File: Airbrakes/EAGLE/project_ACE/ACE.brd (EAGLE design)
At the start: 106.7 x 61 mm, 8 parts, among them J3 PTH

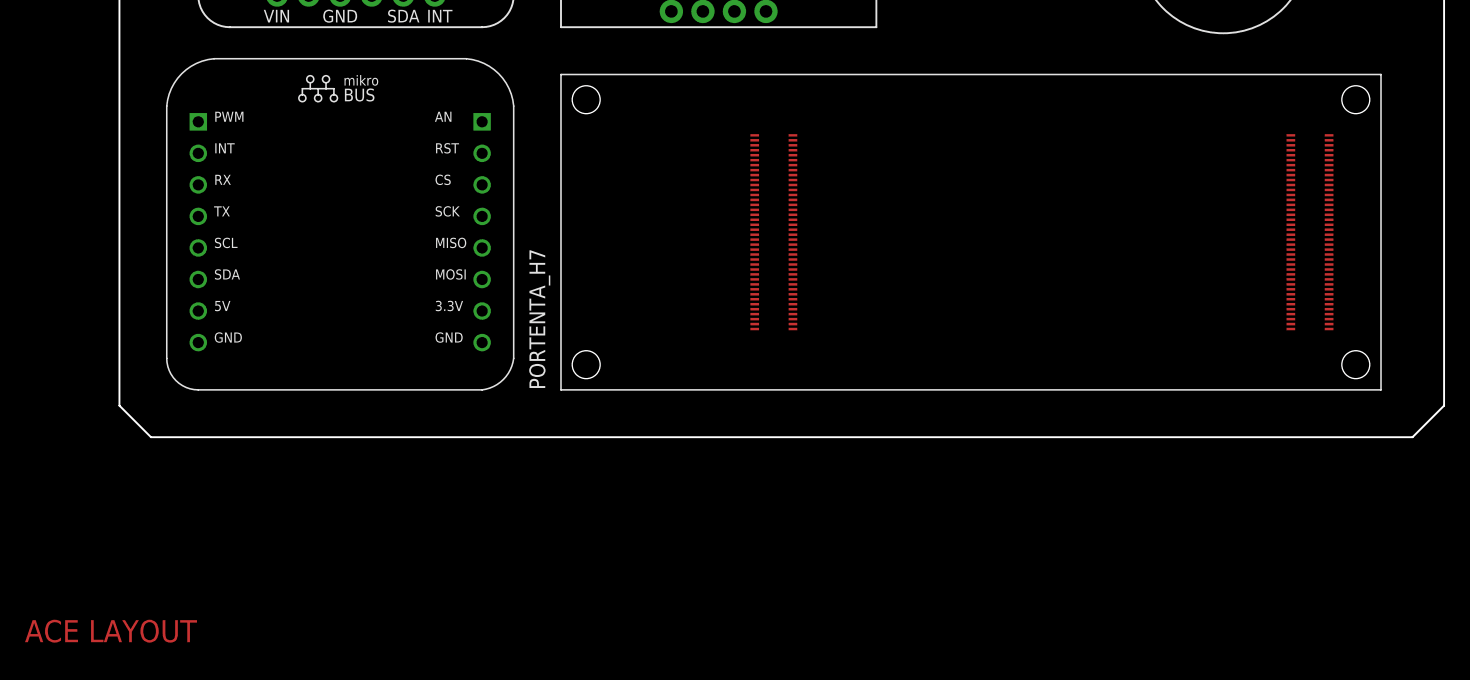
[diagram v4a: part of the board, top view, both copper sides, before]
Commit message: Update schematic and board with Portenta pin headers
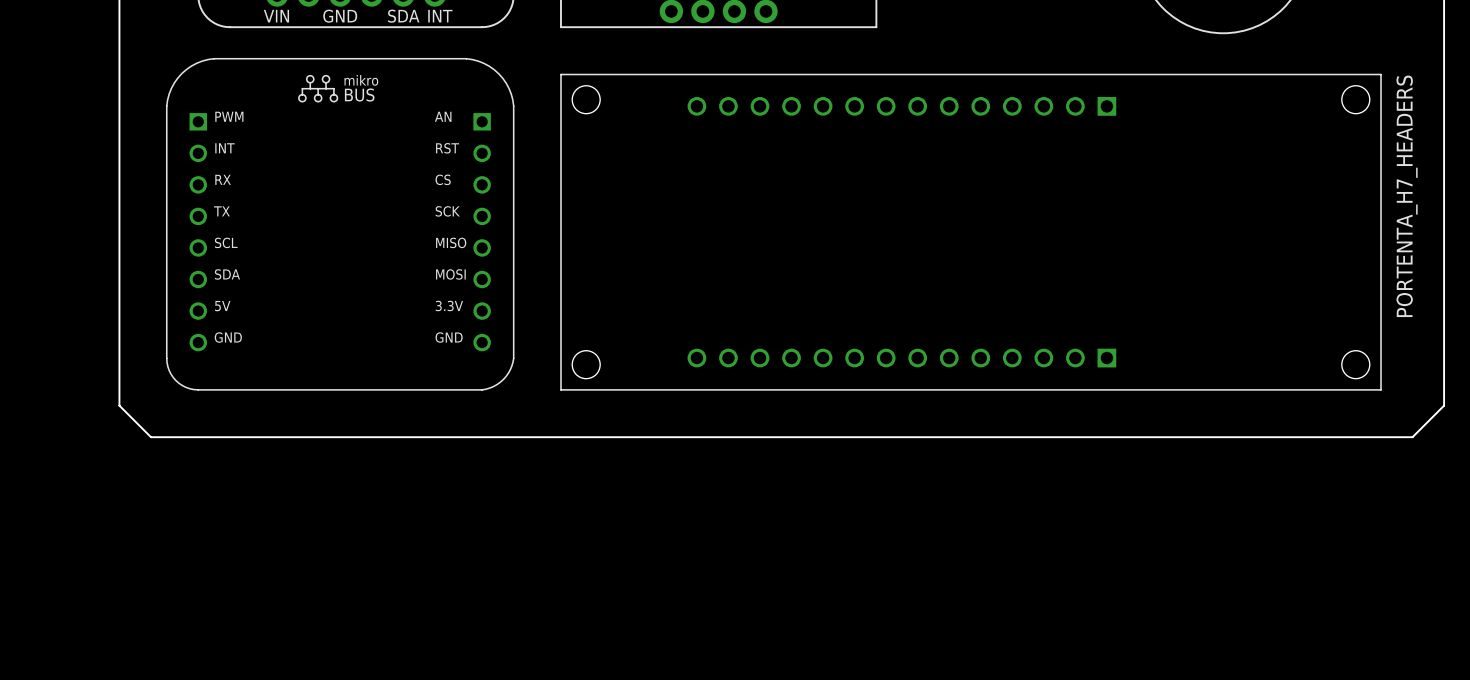
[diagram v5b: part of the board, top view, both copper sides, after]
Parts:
- removed PORTENTA_H7: ABX00042, ABX00042:MODULE_ABX00042
- added U$10: ABX00042_HEADERS_IO, ABX00042:MODULE_ABX00042_HEADERS
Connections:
- removed net GND_1: PORTENTA_H7.J2_24, PORTENTA_H7.J2_33, PORTENTA_H7.J2_44, PORTENTA_H7.J2_57, PORTENTA_H7.J2_70
- removed net USB1_VBUS: PORTENTA_H7.J1_23
- removed net V-SDCARD: PORTENTA_H7.J1_72
- removed net VCC/+3V3: PORTENTA_H7.J2_23, PORTENTA_H7.J2_43, PORTENTA_H7.J2_69
- removed net VSYS: PORTENTA_H7.J1_53, PORTENTA_H7.J1_64
- net 3.3V: now also U$10.J17
- net GND: now also U$10.J18; no longer PORTENTA_H7.J1_22, PORTENTA_H7.J1_31, PORTENTA_H7.J1_42, PORTENTA_H7.J1_47, PORTENTA_H7.J1_54
- net SCL: now also U$10.J22
- net SDA: now also U$10.J23
- net VCC: now also U$10.J16; no longer PORTENTA_H7.J2_34
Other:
- board text removed: "ACE LAYOUT"
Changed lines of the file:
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@@
 <board>
 <plain>
-<text x="12.7" y="-7.62" size="1.778" layer="1">ACE LAYOUT</text>
 <wire x1="20.32" y1="67.31" x2="20.32" y2="11.43" width="0.1524" layer="20"/>
 <wire x1="20.32" y1="11.43" x2="22.86" y2="8.89" width="0.1524" layer="20"/>
@@
 </autorouter>
 <elements>
-<element name="PORTENTA_H7" library="ABX00042" package="MODULE_ABX00042" value="ABX00042" x="88.9" y="25.4" smashed="yes" rot="R90">
-<attribute name="AVAILABILITY" value="In Stock" x="88.9" y="25.4" size="1.778" layer="27" rot="R90" display="off"/>
-<attribute name="CHECK_PRICES" value="https://www.snapeda.com/parts/ABX00042/Arduino/view-part/?ref=eda" x="88.9" y="25.4" size="1.778" layer="27" rot="R90" display="off"/>
-<attribute name="DESCRIPTION" value=" Development Boards &amp; Kits - ARM Portenta H7 | Arduino ABX00042 " x="88.9" y="25.4" size="1.778" layer="27" rot="R90" display="off"/>
-<attribute name="MF" value="Arduino" x="88.9" y="25.4" size="1.778" layer="27" rot="R90" display="off"/>
-<attribute name="MP" value="ABX00042" x="88.9" y="25.4" size="1.778" layer="27" rot="R90" display="off"/>
-<attribute name="NAME" x="54.61" y="12.7" size="1.27" layer="25" rot="R90"/>
-<attribute name="PACKAGE" value="None" x="88.9" y="25.4" size="1.778" layer="27" rot="R90" display="off"/>
-<attribute name="PRICE" value="None" x="88.9" y="25.4" size="1.778" layer="27" rot="R90" display="off"/>
-<attribute name="PURCHASE-URL" value="https://www.snapeda.com/api/url_track_click_mouser/?unipart_id=6801596&amp;manufacturer=Arduino&amp;part_name=ABX00042&amp;search_term=None" x="88.9" y="25.4" size="1.778" layer="27" rot="R90" display="off"/>
-<attribute name="SNAPEDA_LINK" value="https://www.snapeda.com/parts/ABX00042/Arduino/view-part/?ref=snap" x="88.9" y="25.4" size="1.778" layer="27" rot="R90" display="off"/>
-<attribute name="VALUE" x="124.46" y="12.7" size="1.27" layer="27" rot="R90"/>
-</element>
 <element name="J3" library="SparkX" package="1X04_NO_SILK" value="PTH" x="64.77" y="43.18" smashed="yes">
 <attribute name="NAME" x="63.5" y="44.577" size="0.6096" layer="25" font="vector" ratio="20"/>
@@
 <element name="U$19" library="buzzard_labels (13)" package="SCL2" value="" x="72.39" y="44.958" smashed="yes" rot="R90"/>
 <element name="U$5" library="ADAFRUIT_BNO08x" package="ADAFRUIT_BNO08X_FOOTPRINT" value="ADAFRUIT_BNO08X" x="25.4" y="40.64" smashed="yes"/>
+<element name="U$10" library="ABX00042" package="MODULE_ABX00042_HEADERS" value="ABX00042_HEADERS_IO" x="88.9" y="25.4" smashed="yes" rot="R270"/>
 </elements>
 <signals>
-<signal name="USB1_VBUS">
-<contactref element="PORTENTA_H7" pad="J1_23"/>
-</signal>
 <signal name="GND" class="2">
-<contactref element="PORTENTA_H7" pad="J1_22"/>
-<contactref element="PORTENTA_H7" pad="J1_42"/>
-<contactref element="PORTENTA_H7" pad="J1_31"/>
-<contactref element="PORTENTA_H7" pad="J1_54"/>
-<contactref element="PORTENTA_H7" pad="J1_47"/>
 <contactref element="J3" pad="1"/>
 <contactref element="U$1" pad="GND_0"/>
 <contactref element="U$5" pad="GND"/>
-<wire x1="71.48" y1="26.8" x2="64.77" y2="43.18" width="0" layer="19" extent="1-1"/>
-<wire x1="71.48" y1="23.6" x2="71.48" y2="26.8" width="0" layer="19" extent="1-1"/>
-<wire x1="74.56" y1="28" x2="71.48" y2="26.8" width="0" layer="19" extent="1-1"/>
-<wire x1="74.56" y1="25.6" x2="74.56" y2="28" width="0" layer="19" extent="1-1"/>
-<wire x1="74.56" y1="21.6" x2="71.48" y2="23.6" width="0" layer="19" extent="1-1"/>
-<wire x1="26.67" y1="16.51" x2="71.48" y2="23.6" width="0" layer="19" extent="1-1"/>
-<wire x1="38.1" y1="44.45" x2="26.67" y2="16.51" width="0" layer="19" extent="1-1"/>
-</signal>
-<signal name="VSYS">
-<contactref element="PORTENTA_H7" pad="J1_53"/>
-<contactref element="PORTENTA_H7" pad="J1_64"/>
-<wire x1="71.48" y1="28" x2="74.56" y2="30" width="0" layer="19" extent="1-1"/>
-</signal>
-<signal name="V-SDCARD">
-<contactref element="PORTENTA_H7" pad="J1_72"/>
-</signal>
-<signal name="GND_1">
-<contactref element="PORTENTA_H7" pad="J2_33"/>
-<contactref element="PORTENTA_H7" pad="J2_70"/>
-<contactref element="PORTENTA_H7" pad="J2_57"/>
-<contactref element="PORTENTA_H7" pad="J2_44"/>
-<contactref element="PORTENTA_H7" pad="J2_24"/>
-<wire x1="114.66" y1="28.8" x2="117.74" y2="26.8" width="0" layer="19" extent="1-1"/>
-<wire x1="114.66" y1="24.8" x2="117.74" y2="26.8" width="0" layer="19" extent="1-1"/>
-<wire x1="117.74" y1="22" x2="114.66" y2="24.8" width="0" layer="19" extent="1-1"/>
-<wire x1="114.66" y1="19.6" x2="117.74" y2="22" width="0" layer="19" extent="1-1"/>
-</signal>
-<signal name="VCC/+3V3">
-<contactref element="PORTENTA_H7" pad="J2_43"/>
-<contactref element="PORTENTA_H7" pad="J2_69"/>
-<contactref element="PORTENTA_H7" pad="J2_23"/>
-<wire x1="117.74" y1="24.8" x2="117.74" y2="28.8" width="0" layer="19" extent="1-1"/>
-<wire x1="117.74" y1="19.6" x2="117.74" y2="24.8" width="0" layer="19" extent="1-1"/>
+<contactref element="U$10" pad="J18"/>
+<wire x1="38.1" y1="44.45" x2="64.77" y2="43.18" width="0" layer="19" extent="1-1"/>
+<wire x1="26.67" y1="16.51" x2="38.1" y2="44.45" width="0" layer="19" extent="1-1"/>
+<wire x1="92.2274" y1="15.2654" x2="64.77" y2="43.18" width="0" layer="19" extent="1-1"/>
 </signal>
 <signal name="VCC" class="2">
-<contactref element="PORTENTA_H7" pad="J2_34"/>
 <contactref element="U$5" pad="VIN"/>
 <contactref element="U$1" pad="5V"/>
-<wire x1="33.02" y1="44.45" x2="114.66" y2="26.8" width="0" layer="19" extent="1-1"/>
-<wire x1="26.67" y1="19.05" x2="33.02" y2="44.45" width="0" layer="19" extent="1-1"/>
+<contactref element="U$10" pad="J16"/>
+<wire x1="26.67" y1="19.05" x2="97.3074" y2="15.2654" width="0" layer="19" extent="1-1"/>
+<wire x1="33.02" y1="44.45" x2="26.67" y2="19.05" width="0" layer="19" extent="1-1"/>
 </signal>
 <signal name="3.3V" class="2">
@@
 <contactref element="U$5" pad="3VO"/>
 <contactref element="U$1" pad="3.3V"/>
+<contactref element="U$10" pad="J17"/>
 <wire x1="49.53" y1="19.05" x2="67.31" y2="43.18" width="0" layer="19" extent="1-1"/>
+<wire x1="94.7674" y1="15.2654" x2="49.53" y2="19.05" width="0" layer="19" extent="1-1"/>
 <wire x1="35.56" y1="44.45" x2="49.53" y2="19.05" width="0" layer="19" extent="1-1"/>
 </signal>
@@
 <contactref element="U$1" pad="SCL"/>
 <contactref element="U$5" pad="SCL"/>
+<contactref element="U$10" pad="J22"/>
 <wire x1="40.64" y1="44.45" x2="72.39" y2="43.18" width="0" layer="19" extent="1-1"/>
 <wire x1="26.67" y1="24.13" x2="40.64" y2="44.45" width="0" layer="19" extent="1-1"/>
+<wire x1="82.0674" y1="15.2654" x2="72.39" y2="43.18" width="0" layer="19" extent="1-1"/>
 </signal>
 <signal name="SDA">
@@
 <contactref element="U$1" pad="SDA"/>
 <contactref element="U$5" pad="SDA"/>
+<contactref element="U$10" pad="J23"/>
 <wire x1="43.18" y1="44.45" x2="69.85" y2="43.18" width="0" layer="19" extent="1-1"/>
 <wire x1="26.67" y1="21.59" x2="43.18" y2="44.45" width="0" layer="19" extent="1-1"/>
+<wire x1="79.5274" y1="15.2654" x2="69.85" y2="43.18" width="0" layer="19" extent="1-1"/>
 </signal>
 <signal name="N$1" class="2">

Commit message: Update ACE.brd
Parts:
- added 0OHM: (no value), fab_new:R1206
- added PAD1, PAD2: (no value), wirepad:2,15/1,0
- added POWER_TERMINAL: CONN_02_TERM-ADAFRUIT, fab_new:3.5MMTERM
- added R1, R2: 0 ohm, fab_new:R1206
- added SERVO_TERMINAL: CONN_03_TERM'-FABLAB', fab_new:ED555DS-3DS
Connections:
- new net 7.4V: POWER_TERMINAL.2, SERVO_TERMINAL.3
- new net N$2: R1.2, R2.1
- new net PWM: 0OHM.1, 0OHM.2, SERVO_TERMINAL.1, U$10.J9
- net GND: now also PAD1.1, PAD2.1, POWER_TERMINAL.1, R2.2, SERVO_TERMINAL.2
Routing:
- net GND: track 0.00 -> 202.4 mm
- net 3.3V: track 0.00 -> 151.4 mm
- net SCL: track 0.00 -> 132.3 mm
- net SDA: track 0.00 -> 121.8 mm
- net VCC: track 0.00 -> 119.8 mm
- net PWM: track 0.00 -> 37.0 mm
- net 7.4V: track 0.00 -> 25.4 mm
- net N$3: track 0.00 -> 1.27 mm
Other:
- board text removed: "power_terminal"
- board text removed: "servo_terminal"

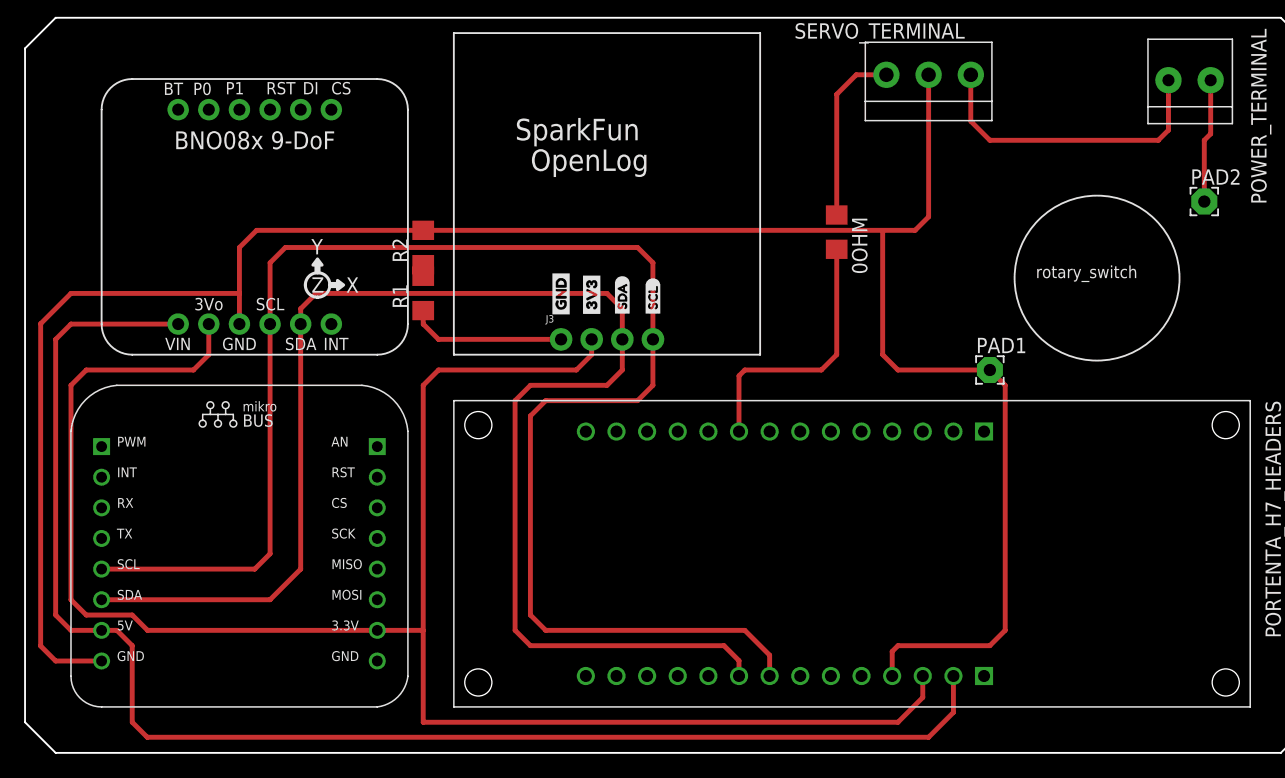
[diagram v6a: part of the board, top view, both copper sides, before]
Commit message: Reroute layout and schematic
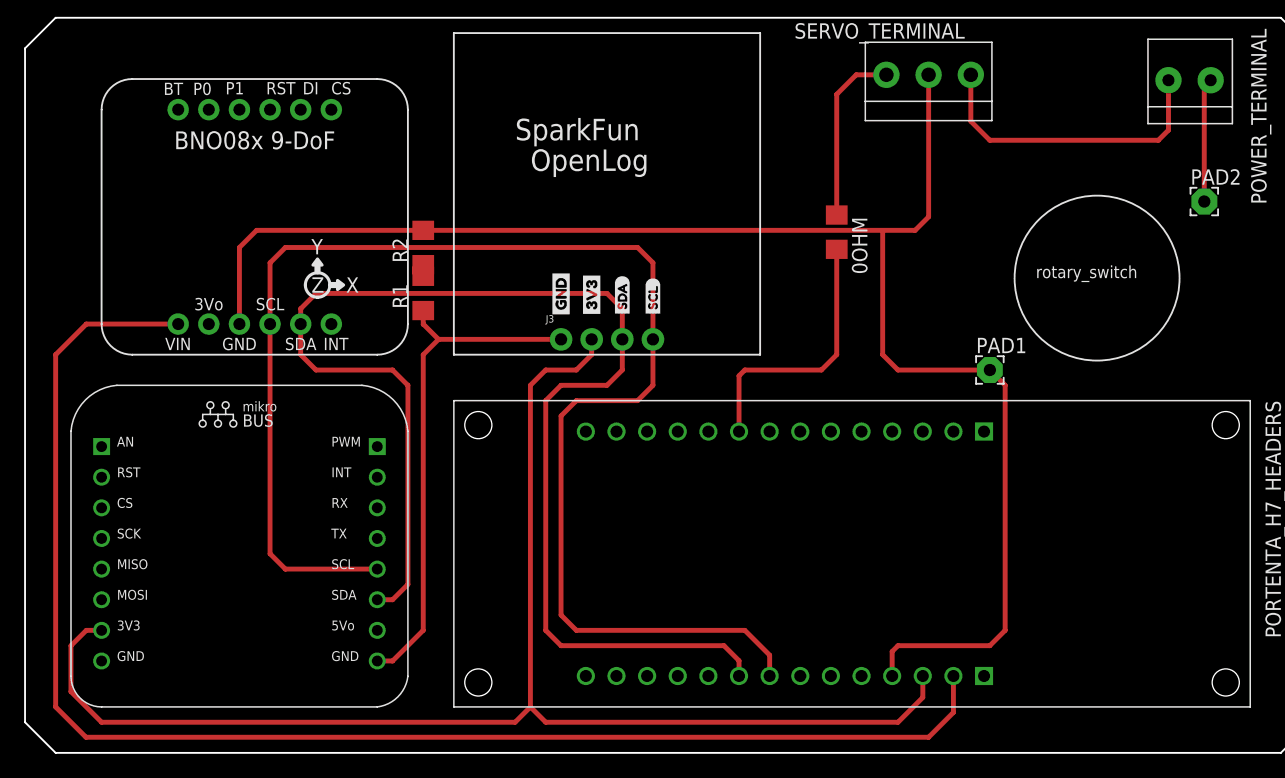
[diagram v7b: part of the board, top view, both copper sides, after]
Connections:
- removed net N$1: U$1.GND_1
- new net N$4: U$1.GND_0
- net 3.3V: now also U$1.3V3; no longer U$1.3.3V, U$5.3VO
- net GND: now also U$1.GND_1; no longer U$1.GND_0
- net VCC: no longer U$1.5V
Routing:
- net 3.3V: track 151.4 -> 116.3 mm
- net GND: track 202.4 -> 182.1 mm
- net SDA: track 121.8 -> 110.9 mm
- net SCL: track 132.3 -> 122.1 mm

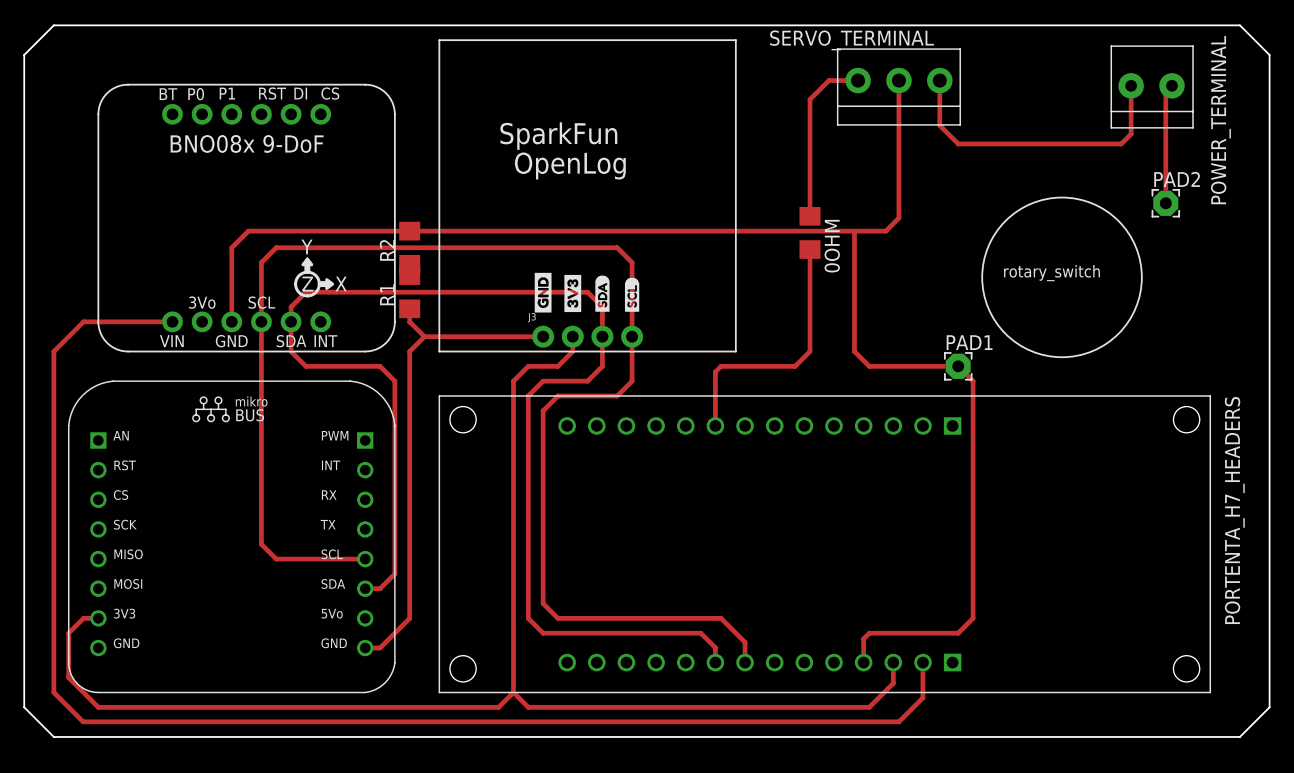
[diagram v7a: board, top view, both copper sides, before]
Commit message: Shrink board width to 100mm
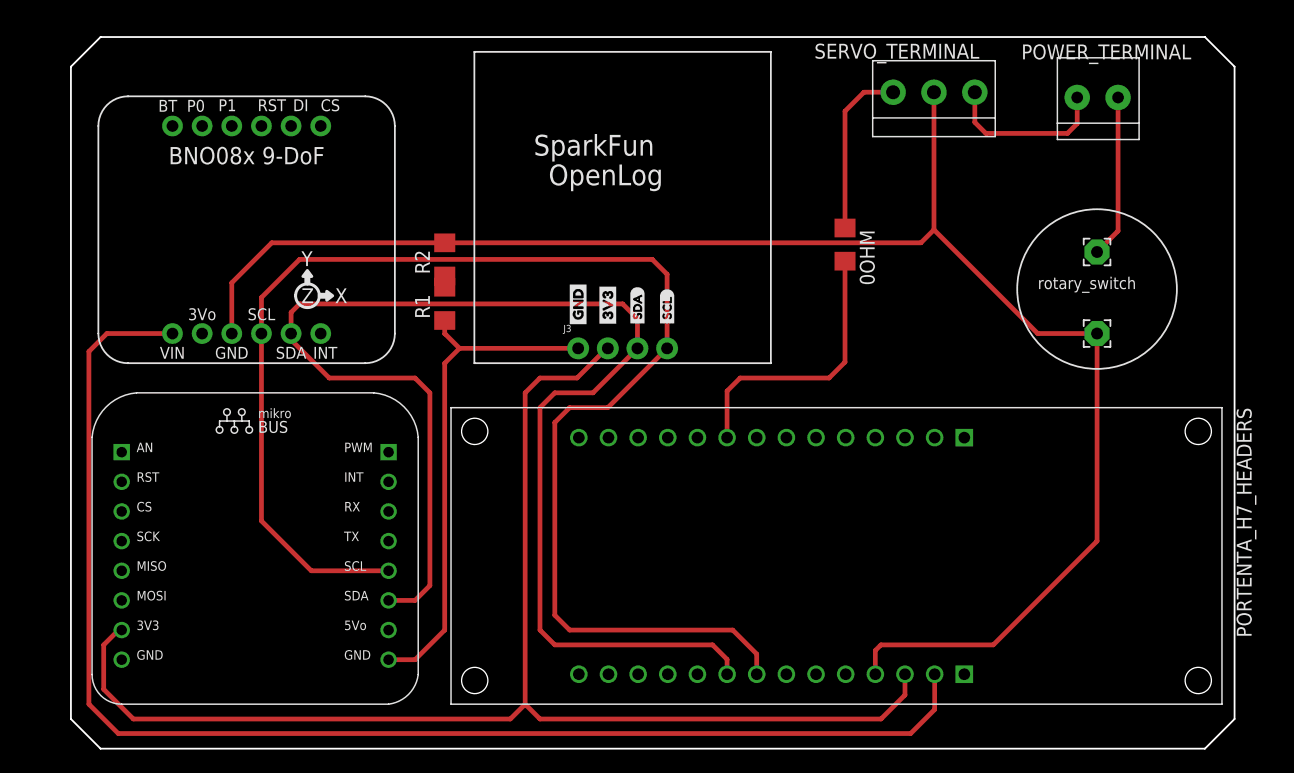
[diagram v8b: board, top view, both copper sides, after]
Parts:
- moved PAD1 12.2 mm to (112.2, 43.5)
- moved PAD2 7.22 mm to (112.2, 50.4)
- moved POWER_TERMINAL 4.73 mm to (112.2, 63.7)
- moved 0OHM 3.16 mm to (90.6, 51.1)
- moved J3 3.16 mm to (67.8, 42.2)
- moved R1 3.16 mm to (56.3, 46.0)
- moved R2 3.16 mm to (56.3, 49.8)
- moved SERVO_TERMINAL 3.16 mm to (98.2, 64.1)
- moved U$16 3.16 mm to (72.8, 44.0)
- moved U$19 3.16 mm to (75.4, 44.0)
- moved U$8 3.16 mm to (70.3, 43.8)
- moved U$9 3.16 mm to (67.8, 43.8)
- moved U$1 2.24 mm to (26.1, 10.4)
- moved U$10 1.41 mm to (89.9, 24.4)
- moved U$5 1.00 mm to (25.4, 39.6)
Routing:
- net GND: track 182.1 -> 195.2 mm
- net 7.4V: track 25.4 -> 14.3 mm
- net SDA: track 110.9 -> 117.6 mm
- net VCC: track 119.8 -> 115.4 mm
- net SCL: track 122.1 -> 123.9 mm
- net 3.3V: track 116.3 -> 114.6 mm
- net PWM: track 37.0 -> 38.6 mm
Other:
- board size 106.7 x 61 mm -> 99.7 x 61 mm
- board text added: "SERVO_TERMINAL"
